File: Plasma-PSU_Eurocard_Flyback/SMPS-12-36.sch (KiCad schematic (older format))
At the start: 55 parts

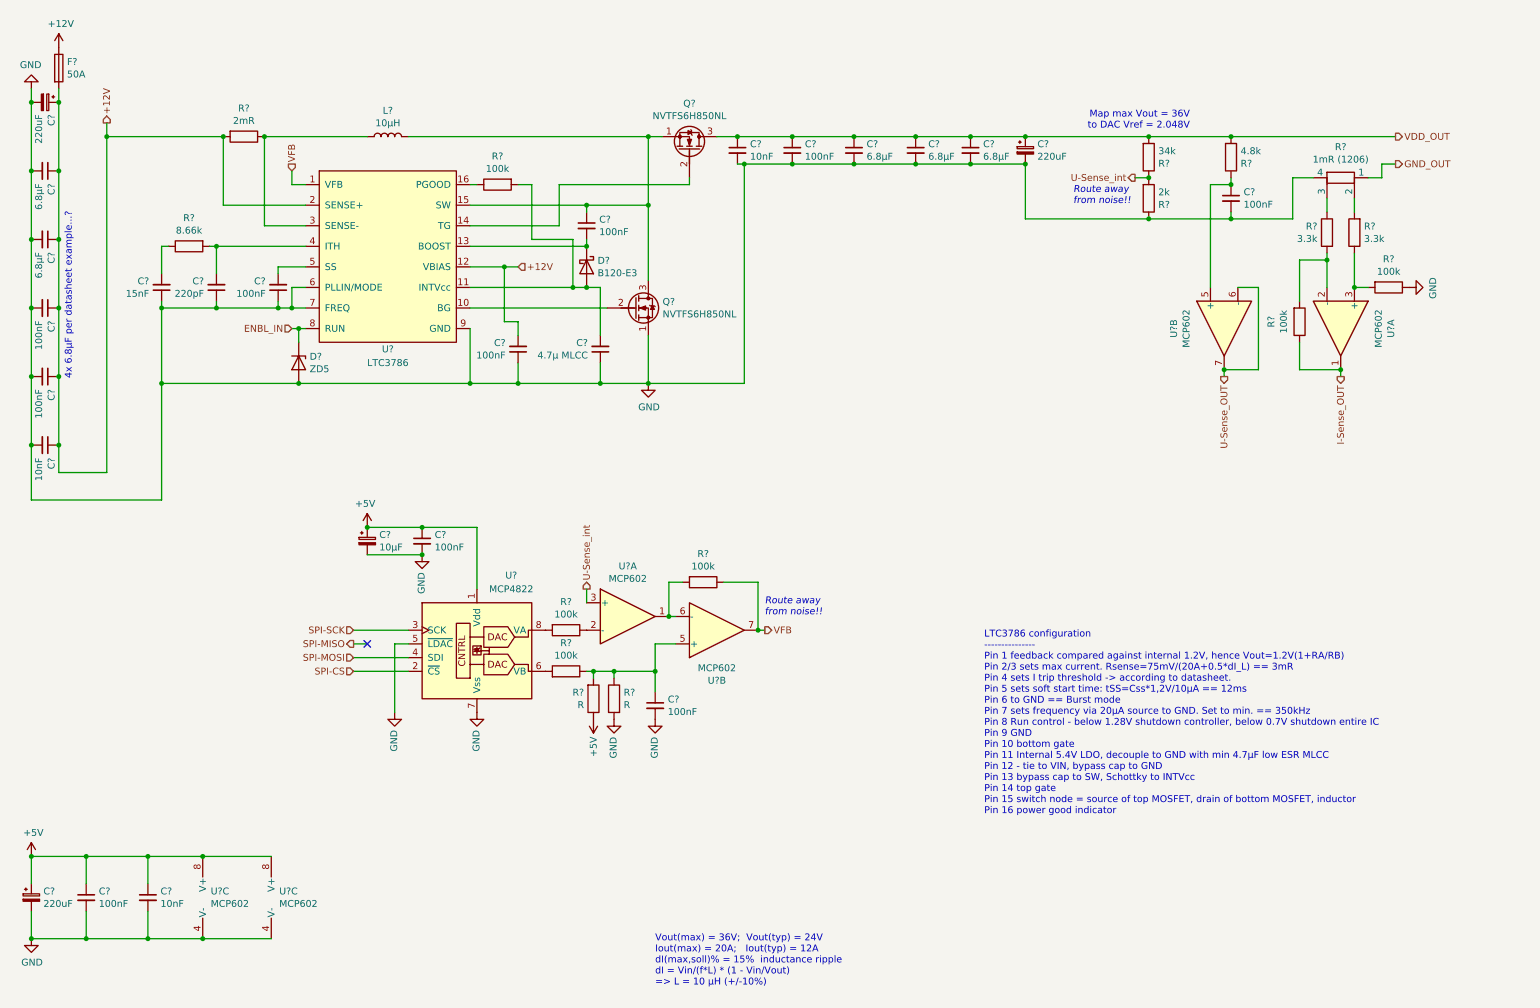
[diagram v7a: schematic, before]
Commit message: Footprints added
All footprints included, except:
- Boost Inductor
- 60A fuse holder
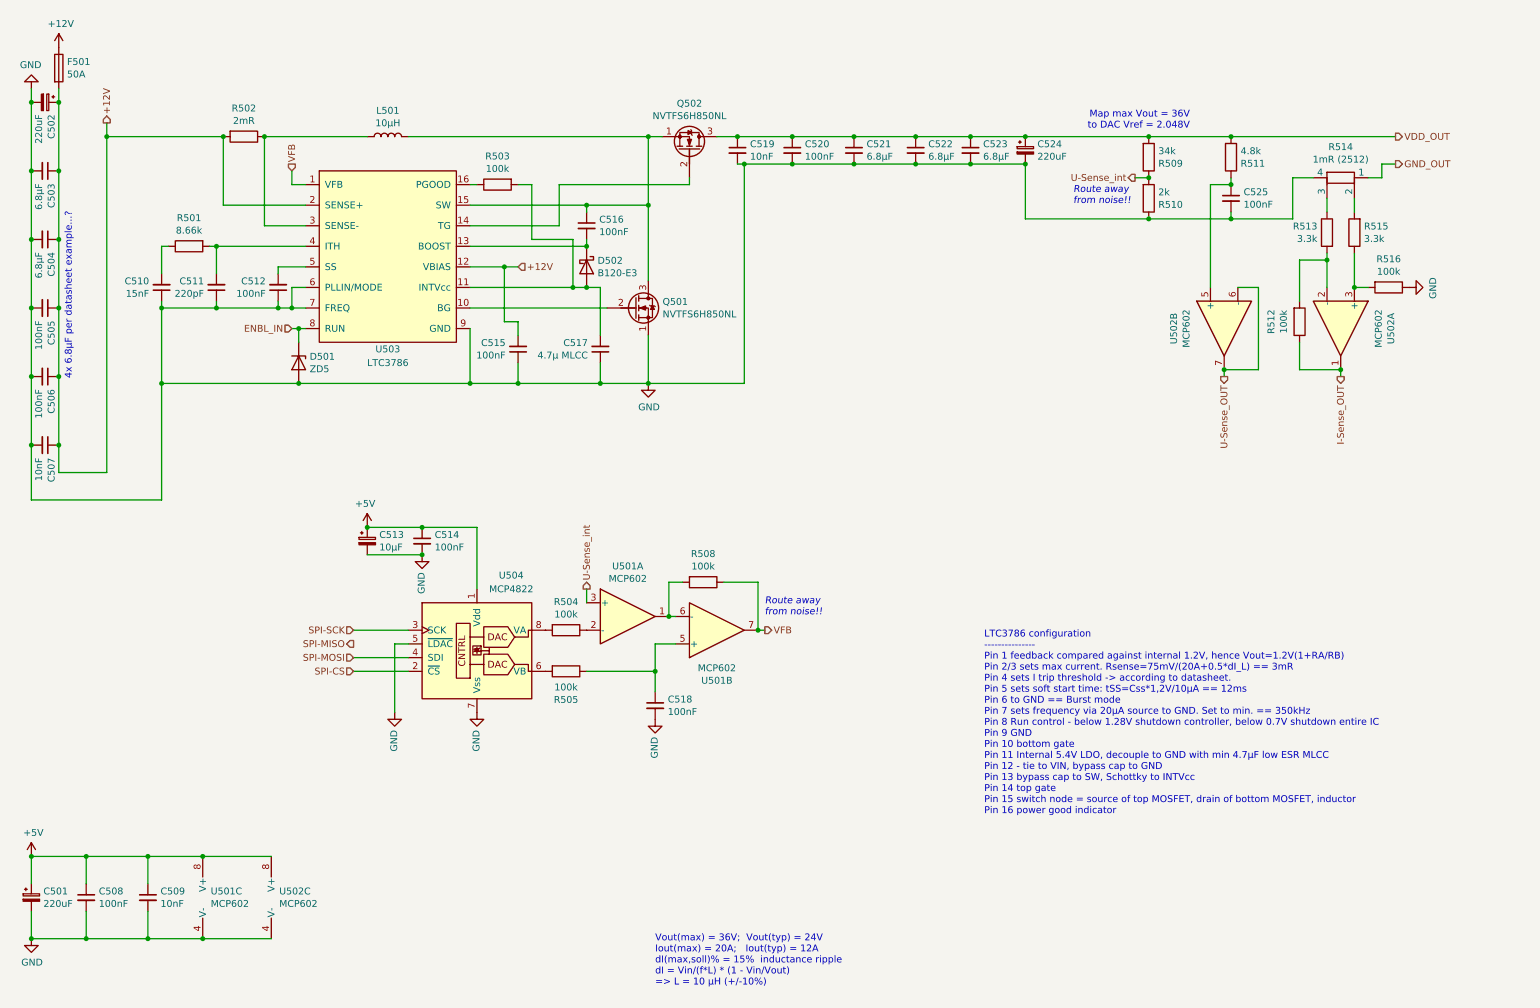
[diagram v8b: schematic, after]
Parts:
- removed R? (x2): R, symbol Device:R
- C501, C502, C524: renamed from C?; footprint (none) -> Capacitor_THT:CP_Radial_D8.0mm_P3.50mm
- C503, C504, C505, C506, C508, C512, C514, C515, C516, C517, C518, C520, C521, C522, C523, C525: renamed from C?; footprint (none) -> Capacitor_SMD:C_1206_3216Metric
- C507, C509, C510, C511, C519: renamed from C?; footprint (none) -> Capacitor_SMD:C_0805_2012Metric
- C513: renamed from C?; footprint (none) -> Capacitor_SMD:C_Elec_6.3x5.8
- D501: renamed from D?; footprint (none) -> Diode_SMD:D_SOD-323
- Q501, Q502: renamed from Q?; footprint (none) -> Plasma-PSU_Eurocard_Flyback:ONSEMI-µ8FL
- R501, R503, R504, R505, R508, R509, R510, R511, R512, R513, R515, R516: renamed from R?; footprint (none) -> Resistor_SMD:R_0805_2012Metric
- R502: renamed from R?; footprint (none) -> Resistor_SMD:R_2512_6332Metric
- R514: renamed from R?; value 1mR (1206) -> 1mR (2512); footprint (none) -> Resistor_SMD:R_2512_6332Metric
- U501, U502, U504: renamed from U?; footprint (none) -> Package_SO:SOIC-8_3.9x4.9mm_P1.27mm
- U503: renamed from U?; footprint (none) -> Package_DFN_QFN:QFN-16-1EP_3x3mm_P0.5mm_EP1.45x1.45mm_ThermalVias
- gave numbers to parts that had none: 3
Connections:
- no-connect marks 1 -> 0
